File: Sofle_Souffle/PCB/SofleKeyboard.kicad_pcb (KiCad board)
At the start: 2 copper layers, 143.3 x 111.7 mm, 99 parts, among them J2 4PIN, J3 OLED, J4 Conn_01x05_Female, P1 i2c_pin, P2 i2c_pin, P3 i2c_pin, P4 i2c_pin, P5 i2c_pin, P6 i2c_pin, P7 i2c_pin, P8 sw_pin, P9 sw_pin, SW1 SW_PUSH-MX_W_LED, SW10 SW_PUSH-MX_W_LED, SW11 SW_PUSH-MX_W_LED, SW12 SW_PUSH-MX_W_LED, SW13 SW_PUSH-MX_W_LED, SW14 SW_PUSH-MX_W_LED, SW15 SW_PUSH-MX_W_LED, SW16 SW_PUSH-MX_W_LED, SW17 SW_PUSH-MX_W_LED, SW18 SW_PUSH-MX_W_LED, SW19 SW_PUSH-MX_W_LED, SW2 SW_PUSH-MX_W_LED, SW20 SW_PUSH-MX_W_LED, SW21 SW_PUSH-MX_W_LED, SW22 SW_PUSH-MX_W_LED, SW23 SW_PUSH-MX_W_LED, SW24 SW_PUSH-MX_W_LED, SW25 Rotary_Encoder_Switch, SW25A1 SW_PUSH-MX_W_LED, SW26 SW_PUSH-MX_W_LED, SW27 SW_PUSH-MX_W_LED, SW28 SW_PUSH-MX_W_LED, SW29 SW_PUSH-MX_W_LED, SW3 SW_PUSH-MX_W_LED, SW30 SW_PUSH-MX_W_LED, SW4 SW_PUSH-MX_W_LED, SW5 SW_PUSH-MX_W_LED, SW6 SW_PUSH-MX_W_LED, SW7 SW_PUSH-MX_W_LED, SW8 SW_PUSH-MX_W_LED, SW9 SW_PUSH-MX_W_LED, U1 ProMicro

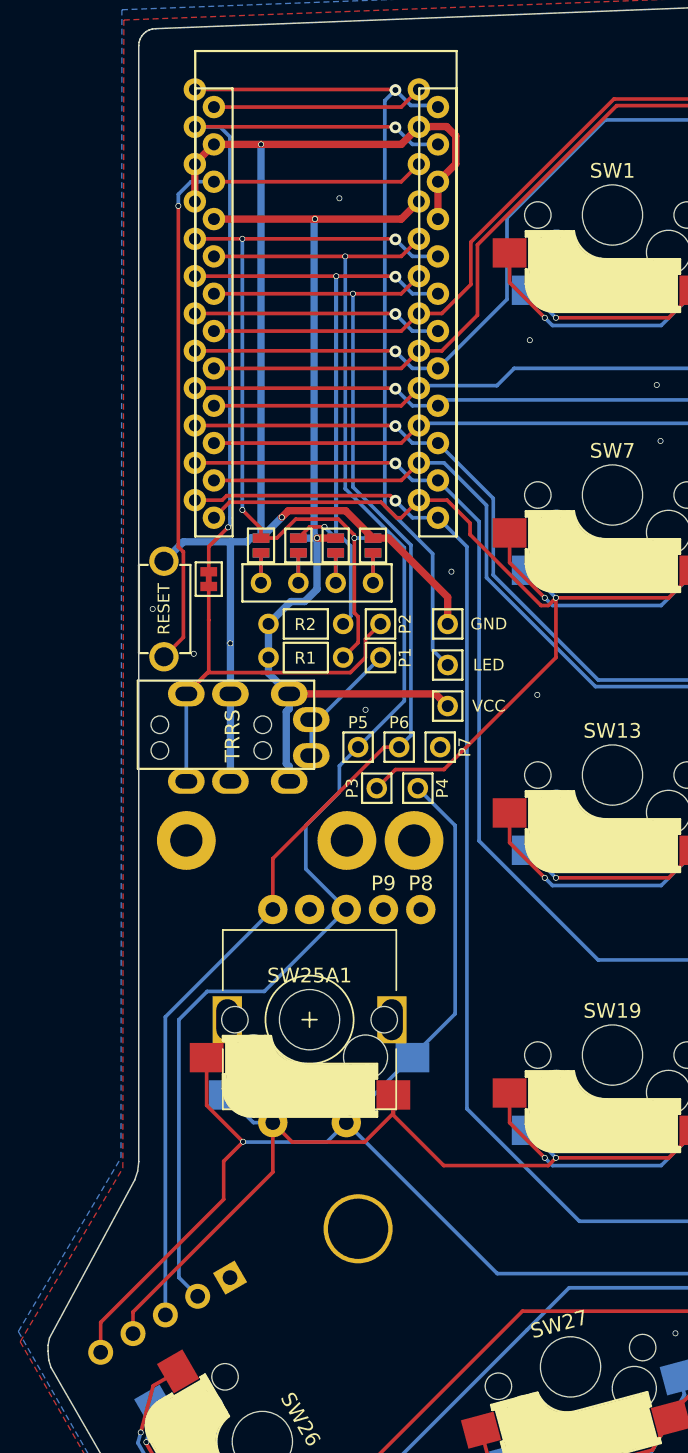
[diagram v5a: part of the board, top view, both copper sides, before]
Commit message: Completed redesign of the roller encoder pins.
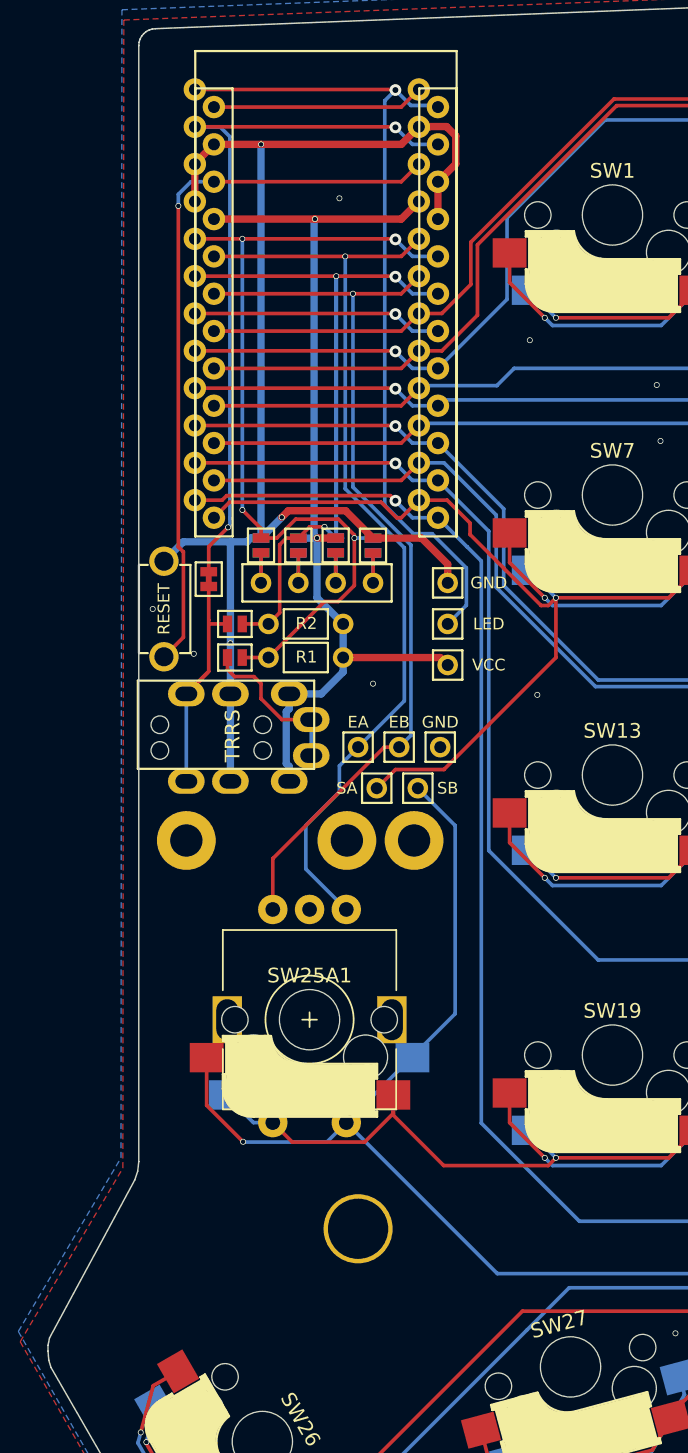
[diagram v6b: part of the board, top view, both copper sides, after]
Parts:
- removed ? (x2): , 
- removed J4: Conn_01x05_Female, Connector_PinHeader_2.54mm:PinHeader_1x05_P2.54mm_Horizontal
- removed P1, P2: i2c_pin, SofleRGB:1pin_conn
- removed P8, P9: sw_pin, SofleRGB:Single_Hole
- added JP10: SolderJumper_2_Open, SofleRGB:Jumper, F.Cu at (88.1, 80.0)
- added JP9: SolderJumper_2_Open, SofleRGB:Jumper, F.Cu at (88.1, 82.3)
- moved GND1 2.79 mm to (102.6, 77.2)
- moved LED1 2.79 mm to (102.6, 80.0)
- moved VCC1 2.79 mm to (102.6, 82.8)
- turned P7 to 0 degrees
- turned R1 to 180 degrees
- turned R2 to 180 degrees
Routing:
- net ENCA: track 98.3 -> 64.4 mm
- net ENCB: track 93.1 -> 62.4 mm
- net SW25B: track 88.3 -> 69.6 mm
- net SW25A: track 207.1 -> 188.9 mm
- net /i2c_d: track 29.1 -> 16.0 mm
- net SDA: track 55.4 -> 59.6 mm
- net VCC: track 69.1 -> 66.4 mm
- net SCL: track 62.2 -> 64.8 mm
- net /i2c_c: track 8.91 -> 11.5 mm
- net GND: track 95.9 -> 94.4 mm, vias 21 -> 19
- net LED: track 58.2 -> 57.2 mm

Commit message: Checkpoint commit.
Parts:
- moved GND1 0.76 mm to (102.6, 78.0)
- moved LED1 0.76 mm to (102.6, 80.8)
- moved VCC1 0.76 mm to (102.6, 83.6)
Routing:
- net LED: track 57.2 -> 58.0 mm
- net GND: track 94.4 -> 95.2 mm
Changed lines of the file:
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@@
       (effects (font (size 1 1) (thickness 0.15)))
     )
-    (fp_text user "D?" (at -5.2 6 120) (layer "B.SilkS") hide
+    (fp_text user "SW26" (at -0.037239 3.098501 -60 unlocked) (layer "B.SilkS") hide
       (effects (font (size 1 1) (thickness 0.15)) (justify mirror))
     )
@@
     (fp_line (start 5.9 -1.1) (end 2.62 -1.1) (layer "F.SilkS") (width 0.15))
     (fp_line (start 5.67 -3.7) (end 5.67 -1.46) (layer "F.SilkS") (width 0.15))
-    (fp_arc (start 0.8 -3.4) (mid 2.26871 -2.886118) (end 3.016318 -1.521471) (layer "F.SilkS") (width 1))
+    (fp_arc (start 0.8 -3.4) (mid 2.268709 -2.886118) (end 3.016318 -1.521471) (layer "F.SilkS") (width 1))
     (fp_arc (start 0.4 -3) (mid 1.868709 -2.486118) (end 2.616318 -1.121471) (layer "F.SilkS") (width 0.15))
     (fp_arc (start 3.8 -6.600001) (mid 5.243504 -6.084925) (end 5.900001 -4.7) (layer "F.SilkS") (width 0.15))
@@
   )
   (footprint "SofleRGB:1pin_conn" (layer "F.Cu")
-    (at 102.616 77.216 -90)
+    (at 102.616 77.978 -90)
     (descr "Resitance 3 pas")
     (tags "R")
@@
   )
   (footprint "SofleRGB:1pin_conn" (layer "F.Cu")
-    (at 102.616 82.804 -90)
+    (at 102.616 83.566 -90)
     (descr "Resitance 3 pas")
     (tags "R")
@@
   )
   (footprint "SofleRGB:1pin_conn" (layer "F.Cu")
-    (at 102.616 80.01 -90)
+    (at 102.616 80.772 -90)
     (descr "Resitance 3 pas")
     (tags "R")
@@
     (property "Sheetname" "")
     (attr through_hole)
-    (fp_text reference "SW25A1" (at 0 3 unlocked) (layer "F.SilkS")
+    (fp_text reference "SW25A1" (at 0 4.064 unlocked) (layer "F.SilkS") hide
       (effects (font (size 1 1) (thickness 0.15)))
     )
@@
       (effects (font (size 1 1) (thickness 0.15)))
     )
-    (fp_text user "D?" (at -5.2 6 180) (layer "B.SilkS") hide
+    (fp_text user "SW25" (at 0 3.81 unlocked) (layer "B.SilkS") hide
       (effects (font (size 1 1) (thickness 0.15)) (justify mirror))
+    )
+    (fp_text user "SW25" (at 0 3.81 180) (layer "F.SilkS")
+      (effects (font (size 1 1) (thickness 0.15)))
     )
     (fp_line (start 4.3 -3.3) (end 2.9 -3.3) (layer "B.SilkS") (width 0.5))
@@
   (segment (start 216.02534 134.62074) (end 212.453079 138.193001) (width 0.25) (layer "B.Cu") (net 35))
   (segment (start 204.995001 138.193001) (end 204.47 137.668) (width 0.25) (layer "B.Cu") (net 35))
-  (segment (start 102.616 75.946) (end 102.616 77.216) (width 0.5) (layer "F.Cu") (net 36))
   (segment (start 97.536 74.17562) (end 95.666369 72.305989) (width 0.5) (layer "F.Cu") (net 36))
   (segment (start 101.371054 46.173744) (end 102.534576 46.173744) (width 0.5) (layer "F.Cu") (net 36))
@@
   (segment (start 101.952815 49.925745) (end 101.952815 52.465745) (width 0.5) (layer "F.Cu") (net 36))
   (segment (start 89.920255 47.385745) (end 99.458255 47.385745) (width 0.5) (layer "F.Cu") (net 36))
+  (segment (start 97.536 74.17562) (end 100.84562 74.17562) (width 0.5) (layer "F.Cu") (net 36))
   (segment (start 86.712815 47.385745) (end 87.996255 47.385745) (width 0.5) (layer "F.Cu") (net 36))
   (segment (start 85.414 48.73) (end 85.414 48.68456) (width 0.5) (layer "F.Cu") (net 36))
   (segment (start 87.996255 47.385745) (end 89.920255 47.385745) (width 0.5) (layer "F.Cu") (net 36))
-  (segment (start 97.536 74.17562) (end 100.84562 74.17562) (width 0.5) (layer "F.Cu") (net 36))
+  (segment (start 100.84562 74.17562) (end 102.616 75.946) (width 0.5) (layer "F.Cu") (net 36))
   (segment (start 103.164816 46.803984) (end 103.164816 48.713744) (width 0.5) (layer "F.Cu") (net 36))
   (segment (start 101.354798 46.19) (end 101.371054 46.173744) (width 0.5) (layer "F.Cu") (net 36))
   (segment (start 95.666369 72.305989) (end 91.778011 72.305989) (width 0.5) (layer "F.Cu") (net 36))
+  (segment (start 102.616 75.946) (end 102.616 77.978) (width 0.5) (layer "F.Cu") (net 36))
   (segment (start 103.164816 48.713744) (end 101.952815 49.925745) (width 0.5) (layer "F.Cu") (net 36))
   (segment (start 100.654 46.19) (end 101.354798 46.19) (width 0.5) (layer "F.Cu") (net 36))
   (segment (start 85.414 51.27) (end 85.414 48.73) (width 0.5) (layer "F.Cu") (net 36))
   (segment (start 85.414 48.68456) (end 86.712815 47.385745) (width 0.5) (layer "F.Cu") (net 36))
-  (segment (start 100.84562 74.17562) (end 102.616 75.946) (width 0.5) (layer "F.Cu") (net 36))
   (via (at 89.920255 47.385745) (size 0.4) (drill 0.3) (layers "F.Cu" "B.Cu") (net 36))
   (via (at 91.328001 72.755999) (size 0.4) (drill 0.3) (layers "F.Cu" "B.Cu") (net 36))
@@
   (segment (start 87.834 84.768) (end 87.834 81.33) (width 0.5) (layer "B.Cu") (net 36))
   (segment (start 87.884 74.422) (end 88.963758 74.422) (width 0.5) (layer "B.Cu") (net 36))
-  (segment (start 102.108 82.296) (end 102.616 82.804) (width 0.5) (layer "F.Cu") (net 37))
+  (segment (start 101.346 82.296) (end 102.616 83.566) (width 0.5) (layer "F.Cu") (net 37))
   (segment (start 93.584255 52.465745) (end 99.458255 52.465745) (width 0.5) (layer "F.Cu") (net 37))
   (segment (start 94.996 74.168) (end 93.726 74.168) (width 0.5) (layer "F.Cu") (net 37))
-  (segment (start 95.504 82.296) (end 102.108 82.296) (width 0.5) (layer "F.Cu") (net 37))
+  (segment (start 95.504 82.296) (end 101.346 82.296) (width 0.5) (layer "F.Cu") (net 37))
   (segment (start 86.712815 52.465745) (end 93.584255 52.465745) (width 0.5) (layer "F.Cu") (net 37))
   (segment (start 99.458255 52.465745) (end 100.654 51.27) (width 0.5) (layer "F.Cu") (net 37))
@@
   (segment (start 85.414 43.65) (end 99.022 43.65) (width 0.25) (layer "F.Cu") (net 55))
   (via (at 99.06 43.688) (size 0.8) (drill 0.4) (layers "F.Cu" "B.Cu") (net 55))
-  (segment (start 100.279642 73.872256) (end 101.558256 73.872256) (width 0.25) (layer "B.Cu") (net 55))
   (segment (start 99.06 43.688) (end 100.109001 44.737001) (width 0.25) (layer "B.Cu") (net 55))
   (segment (start 98.334999 44.413001) (end 98.334999 71.927613) (width 0.25) (layer "B.Cu") (net 55))
-  (segment (start 103.886 78.74) (end 102.616 80.01) (width 0.25) (layer "B.Cu") (net 55))
-  (segment (start 103.886 76.2) (end 103.886 78.74) (width 0.25) (layer "B.Cu") (net 55))
+  (segment (start 103.886 79.502) (end 102.616 80.772) (width 0.25) (layer "B.Cu") (net 55))
+  (segment (start 100.279642 73.872256) (end 101.558256 73.872256) (width 0.25) (layer "B.Cu") (net 55))
+  (segment (start 98.334999 71.927613) (end 100.279642 73.872256) (width 0.25) (layer "B.Cu") (net 55))
   (segment (start 101.844071 44.737001) (end 101.952815 44.845745) (width 0.25) (layer "B.Cu") (net 55))
-  (segment (start 98.334999 71.927613) (end 100.279642 73.872256) (width 0.25) (layer "B.Cu") (net 55))
+  (segment (start 101.558256 73.872256) (end 103.886 76.2) (width 0.25) (layer "B.Cu") (net 55))
+  (segment (start 103.886 76.2) (end 103.886 79.502) (width 0.25) (layer "B.Cu") (net 55))
+  (segment (start 99.06 43.688) (end 98.334999 44.413001) (width 0.25) (layer "B.Cu") (net 55))
   (segment (start 100.109001 44.737001) (end 101.844071 44.737001) (width 0.25) (layer "B.Cu") (net 55))
-  (segment (start 101.558256 73.872256) (end 103.886 76.2) (width 0.25) (layer "B.Cu") (net 55))
-  (segment (start 99.06 43.688) (end 98.334999 44.413001) (width 0.25) (layer "B.Cu") (net 55))
   (segment (start 99.022 46.19) (end 99.06 46.228) (width 0.25) (layer "F.Cu") (net 56))
   (segment (start 86.36 76.46162) (end 86.36 74.752062) (width 0.25) (layer "F.Cu") (net 56))
